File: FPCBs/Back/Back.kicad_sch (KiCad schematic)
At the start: 3 parts, among them J1 Conn_01x18_Pin, SW1 SW_SP5T_NR01105

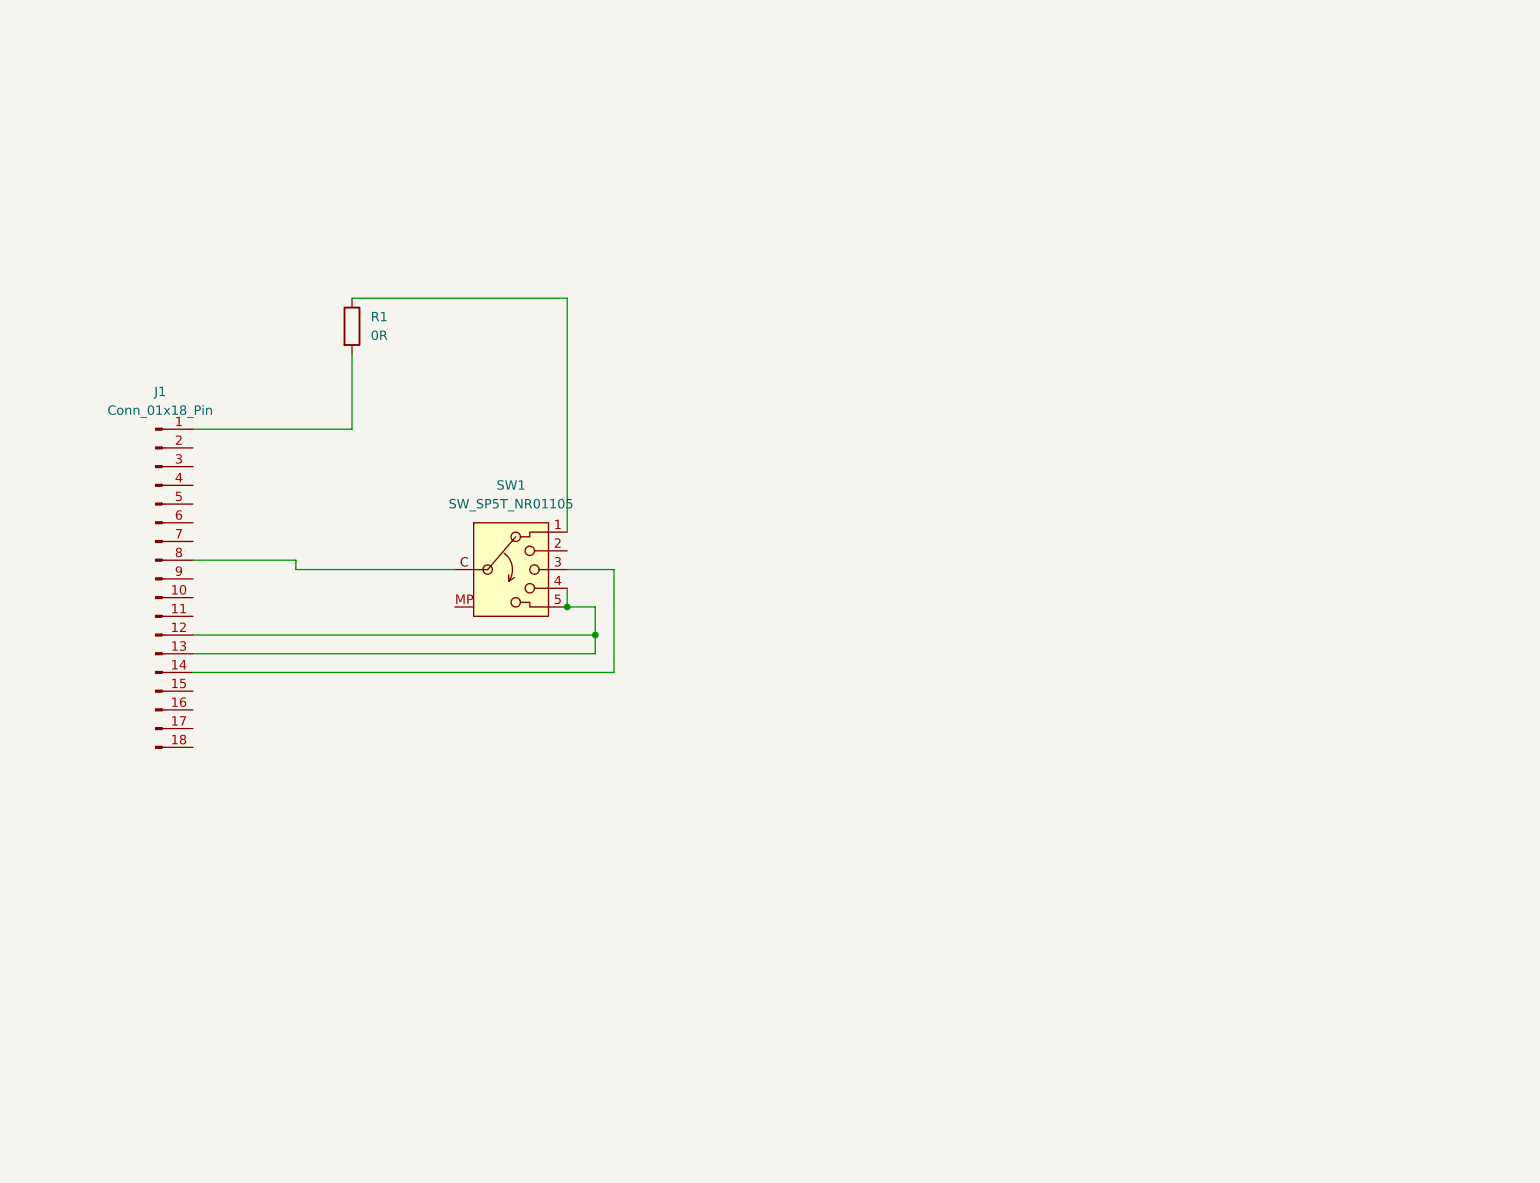
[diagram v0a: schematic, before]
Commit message: Update the back pcb
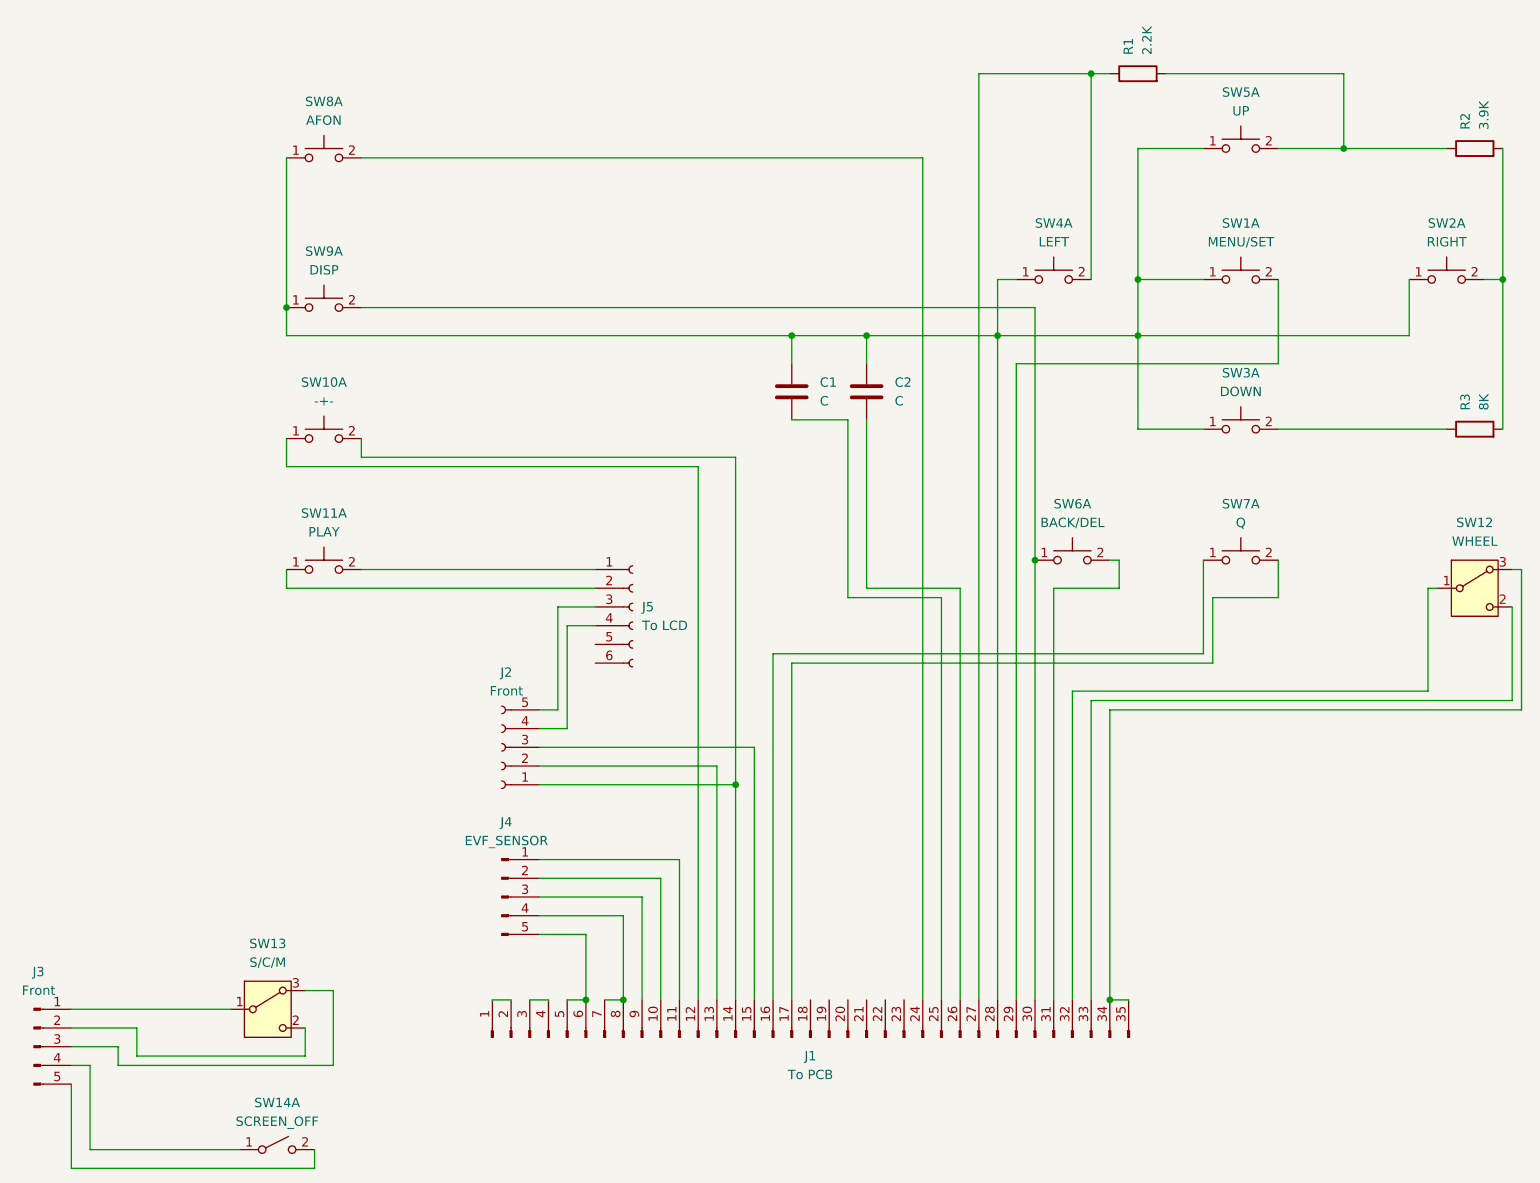
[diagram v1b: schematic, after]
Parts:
- removed J1: Conn_01x18_Pin, Connector_PinHeader_1.00mm:PinHeader_1x18_P1.00mm_Vertical_SMD_Pin1Left, symbol Connector:Conn_01x18_Pin
- removed SW1: SW_SP5T_NR01105, Button_Switch_THT:SW_NKK_NR01, symbol Switch:SW_SP5T_NR01105
- added C1, C2: C, Capacitor_SMD:C_0201_0603Metric, symbol Device:C
- added J1: To PCB, Leica-G9ii:FPC-2Rows-35Pins-0.23mm, symbol Connector:Conn_01x35_Pin
- added J2: Front, symbol Connector:Conn_01x05_Socket
- added J3: Front, symbol Connector:Conn_01x05_Pin
- added J4: EVF_SENSOR, Leica-G9ii:FPC-1Row-7Pins-0.38mm, symbol Connector:Conn_01x05_Pin
- added J5: To LCD, symbol Connector:Conn_01x06_Socket
- added R2: 3.9K, Resistor_SMD:R_0201_0603Metric, symbol Device:R
- added R3: 8K, Resistor_SMD:R_0201_0603Metric, symbol Device:R
- added SW1: MENU/SET, Leica-G9ii:Push_Button, symbol Switch:SW_Push_Dual_x2
- added SW10: -+-, Leica-G9ii:Push_Button, symbol Switch:SW_Push_Dual_x2
- added SW11: PLAY, Leica-G9ii:Push_Button, symbol Switch:SW_Push_Dual_x2
- added SW12: WHEEL, Button_Switch_THT:SW_Slide-03_Wuerth-WS-SLTV_10x2.5x6.4_P2.54mm, symbol Switch:SW_Wuerth_450301014042
- added SW13: S/C/M, Button_Switch_THT:SW_Slide-03_Wuerth-WS-SLTV_10x2.5x6.4_P2.54mm, symbol Switch:SW_Wuerth_450301014042
- added SW14: SCREEN_OFF, symbol Switch:SW_DPST_x2
- added SW2: RIGHT, Leica-G9ii:Push_Button, symbol Switch:SW_Push_Dual_x2
- added SW3: DOWN, Leica-G9ii:Push_Button, symbol Switch:SW_Push_Dual_x2
- added SW4: LEFT, Leica-G9ii:Push_Button, symbol Switch:SW_Push_Dual_x2
- added SW5: UP, Leica-G9ii:Push_Button, symbol Switch:SW_Push_Dual_x2
- added SW6: BACK/DEL, Leica-G9ii:Push_Button, symbol Switch:SW_Push_Dual_x2
- added SW7: Q, Leica-G9ii:Push_Button, symbol Switch:SW_Push_Dual_x2
- added SW8: AFON, Leica-G9ii:Push_Button, symbol Switch:SW_Push_Dual_x2
- added SW9: DISP, Leica-G9ii:Push_Button, symbol Switch:SW_Push_Dual_x2
- R1: value 0R -> 2.2K
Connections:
- net at R1.1: now also J1.27 (Pin_27), SW4.2 (D)
- net at R1.2: now also R2.1, SW5.2 (D)
- new net: C1.1, C2.1, J1.28 (Pin_28), SW1.1 (C), SW2.1 (C), SW3.1 (C), SW4.1 (C), SW5.1 (C), SW8.1 (C), SW9.1 (C)
- new net: C2.2, J1.26 (Pin_26)
- new net: J1.30 (Pin_30), SW6.1 (C), SW9.2 (D)
- new net: R2.2, R3.2, SW2.2 (D)
- new net: J1.32 (Pin_32), SW12.1 (B)
- new net: J1.33 (Pin_33), SW12.2 (C)
- new net: J1.34 (Pin_34), J1.35 (Pin_35), SW12.3 (A)
- new net: J1.31 (Pin_31), SW6.2 (D)
- new net: J5.2 (Pin_2), SW11.1 (C)
- new net: J5.1 (Pin_1), SW11.2 (D)
- new net: J2.5 (Pin_5), J5.3 (Pin_3)
- new net: J2.4 (Pin_4), J5.4 (Pin_4)
- new net: J3.1 (Pin_1), SW13.1 (B)
- new net: J3.2 (Pin_2), SW13.2 (C)
- new net: J3.3 (Pin_3), SW13.3 (A)
- new net: J3.4 (Pin_4), SW14.1 (A)
- new net: J3.5 (Pin_5), SW14.2 (B)
- new net: J1.24 (Pin_24), SW8.2 (D)
- new net: C1.2, J1.25 (Pin_25)
- new net: J1.12 (Pin_12), SW10.1 (C)
- new net: J1.14 (Pin_14), J2.1 (Pin_1), SW10.2 (D)
- new net: R3.1, SW3.2 (D)
- new net: J1.13 (Pin_13), J2.2 (Pin_2)
- new net: J1.15 (Pin_15), J2.3 (Pin_3)
- new net: J1.29 (Pin_29), SW1.2 (D)
- new net: J1.1 (Pin_1), J1.2 (Pin_2)
- new net: J1.10 (Pin_10), J4.2 (Pin_2)
- new net: J1.11 (Pin_11), J4.1 (Pin_1)
- new net: J1.16 (Pin_16), SW7.1 (C)
- new net: J1.17 (Pin_17), SW7.2 (D)
- new net: J1.3 (Pin_3), J1.4 (Pin_4)
- new net: J1.5 (Pin_5), J1.6 (Pin_6), J4.5 (Pin_5)
- new net: J1.7 (Pin_7), J1.8 (Pin_8), J4.4 (Pin_4)
- new net: J1.9 (Pin_9), J4.3 (Pin_3)

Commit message: Add sd card
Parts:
- J2: value Front -> To Front
- J3: footprint (none) -> Leica-G9ii:FPC-1Row-7Pins-0.38mm
- J5: value To LCD -> From LCD
- SW13: footprint Button_Switch_THT:SW_Slide-03_Wuerth-WS-SLTV_10x2.5x6.4_P2.54mm -> Leica-G9ii:Switch_Detection_Bidirectional
- SW14: footprint (none) -> Leica-G9ii:Switch_Detection
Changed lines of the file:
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@@
 			)
 		)
-		(property "Value" "To LCD"
+		(property "Value" "From LCD"
 			(at 107.95 101.5999 0)
 			(effects
@@
 			)
 		)
-		(property "Footprint" ""
+		(property "Footprint" "Leica-G9ii:FPC-1Row-7Pins-0.38mm"
 			(at 25.4 158.75 0)
 			(effects
@@
 			)
 		)
-		(property "Footprint" "Button_Switch_THT:SW_Slide-03_Wuerth-WS-SLTV_10x2.5x6.4_P2.54mm"
+		(property "Footprint" "Leica-G9ii:Switch_Detection_Bidirectional"
 			(at 57.15 163.83 0)
 			(effects
@@
 			)
 		)
-		(property "Datasheet" "https://www.we-online.com/components/products/datasheet/450301014042.pdf"
+		(property "Datasheet" ""
 			(at 57.15 161.29 0)
 			(effects
@@
 			)
 		)
-		(property "Footprint" ""
+		(property "Footprint" "Leica-G9ii:Switch_Detection"
 			(at 58.42 172.72 0)
 			(effects
@@
 			)
 		)
-		(property "Value" "Front"
+		(property "Value" "To Front"
 			(at 89.535 110.49 0)
 			(effects

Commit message: Fixes for the back pcb
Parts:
- C1, C2: footprint Capacitor_SMD:C_0201_0603Metric -> Leica-G9ii:R_2x1mm
- J1: footprint Leica-G9ii:FPC-2Rows-35Pins-0.23mm -> Leica-G9ii:FPC-2Rows-35Pins-0.5mm
- J2: footprint (none) -> Leica-G9ii:Connector-1Row-5Pins-0.40mm
- J3: footprint Leica-G9ii:FPC-1Row-7Pins-0.38mm -> Leica-G9ii:FPC-1Row-5Pins-0.40mm
- J4: footprint Leica-G9ii:FPC-1Row-7Pins-0.38mm -> Leica-G9ii:FPC-1Row-7Pins-0.40mm
- J5: footprint (none) -> Leica-G9ii:Connector-1Row-6Pins-0.40mm
- R1, R2, R3: footprint Resistor_SMD:R_0201_0603Metric -> Leica-G9ii:R_2x1mm
- SW12: footprint Button_Switch_THT:SW_Slide-03_Wuerth-WS-SLTV_10x2.5x6.4_P2.54mm -> Leica-G9ii:Connector-1Row-5Pins-0.40mm
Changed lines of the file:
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@@
 			)
 		)
-		(property "Footprint" "Resistor_SMD:R_0201_0603Metric"
+		(property "Footprint" "Leica-G9ii:R_2x1mm"
 			(at 175.26 28.448 90)
 			(effects
@@
 			)
 		)
-		(property "Footprint" "Capacitor_SMD:C_0201_0603Metric"
+		(property "Footprint" "Leica-G9ii:R_2x1mm"
 			(at 139.3952 73.66 0)
 			(effects
@@
 			)
 		)
-		(property "Footprint" "Button_Switch_THT:SW_Slide-03_Wuerth-WS-SLTV_10x2.5x6.4_P2.54mm"
+		(property "Footprint" "Leica-G9ii:Connector-1Row-5Pins-0.40mm"
 			(at 220.98 106.68 0)
 			(effects
@@
 			)
 		)
-		(property "Datasheet" "https://www.we-online.com/components/products/datasheet/450301014042.pdf"
+		(property "Datasheet" ""
 			(at 220.98 104.14 0)
 			(effects
@@
 			)
 		)
-		(property "Footprint" "Resistor_SMD:R_0201_0603Metric"
+		(property "Footprint" "Leica-G9ii:R_2x1mm"
 			(at 220.98 38.608 90)
 			(effects
@@
 			)
 		)
-		(property "Footprint" ""
+		(property "Footprint" "Leica-G9ii:Connector-1Row-6Pins-0.40mm"
 			(at 106.68 99.06 0)
 			(effects
@@
 			)
 		)
-		(property "Footprint" "Leica-G9ii:FPC-1Row-7Pins-0.38mm"
+		(property "Footprint" "Leica-G9ii:FPC-1Row-5Pins-0.40mm"
 			(at 25.4 158.75 0)
 			(effects
@@
 			)
 		)
-		(property "Footprint" "Capacitor_SMD:C_0201_0603Metric"
+		(property "Footprint" "Leica-G9ii:R_2x1mm"
 			(at 129.2352 73.66 0)
 			(effects
@@
 			)
 		)
-		(property "Footprint" "Resistor_SMD:R_0201_0603Metric"
+		(property "Footprint" "Leica-G9ii:R_2x1mm"
 			(at 220.98 76.708 90)
 			(effects
@@
 			)
 		)
-		(property "Footprint" ""
+		(property "Footprint" "Leica-G9ii:Connector-1Row-5Pins-0.40mm"
 			(at 88.9 118.11 0)
 			(effects
@@
 			)
 		)
-		(property "Footprint" "Leica-G9ii:FPC-2Rows-35Pins-0.23mm"
+		(property "Footprint" "Leica-G9ii:FPC-2Rows-35Pins-0.5mm"
 			(at 130.81 157.48 0)
 			(effects
@@
 			)
 		)
-		(property "Footprint" "Leica-G9ii:FPC-1Row-7Pins-0.38mm"
+		(property "Footprint" "Leica-G9ii:FPC-1Row-7Pins-0.40mm"
 			(at 88.9 138.43 0)
 			(effects

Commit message: Fix the buttons pins
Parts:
- SW12: footprint Leica-G9ii:Connector-1Row-5Pins-0.40mm -> Leica-G9ii:back_dial
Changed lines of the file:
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@@
 			)
 		)
-		(property "Footprint" "Leica-G9ii:Connector-1Row-5Pins-0.40mm"
+		(property "Footprint" "Leica-G9ii:back_dial"
 			(at 220.98 106.68 0)
 			(effects
